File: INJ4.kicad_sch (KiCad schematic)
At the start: 8 parts, among them Q1 VND14NV04-E, Q2 VND14NV04-E, Q3 VND14NV04-E, Q4 VND14NV04-E

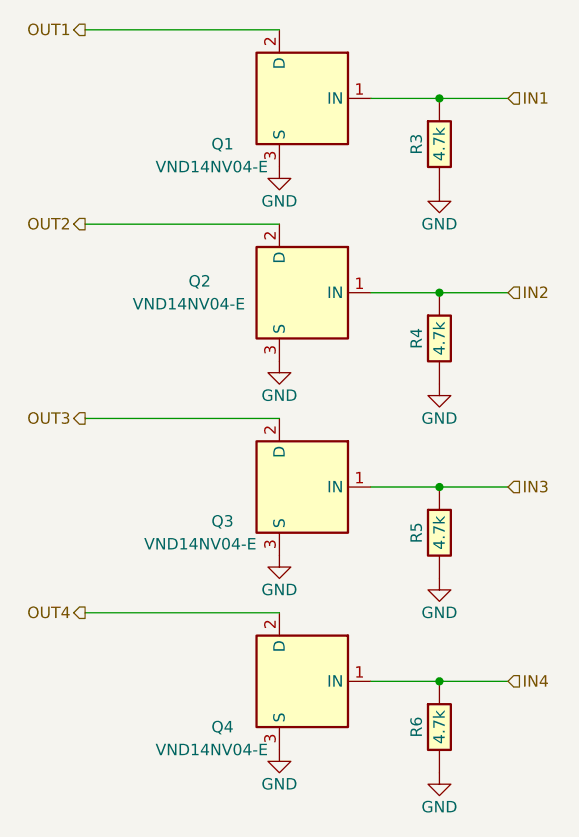
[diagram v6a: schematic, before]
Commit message: EmbeddedEra libraries and template, KiCad 10
- Every symbol except the nine Hellen-One modules now comes from the EmbeddedEra library (resistors and 0R links from the generic libraries, PTC fuses, VND14NV04-E, TE 1-1376430-0, Molex 39281143, test pads, proto area, power symbols). Same-pin parts swapped in place; resistors re-placed between their old pin points with short wires. New parts live on library branch sti2004-parts.
- EmbeddedEra project template: worksheet, text variables, net classes with explicit power classes, JLCPCB design rules; template net names for USB, I2C and the K-line UART.
- Migrated all sheets and the board to KiCad 10 (10.0.7).
- tools/sch_overlap_check.py also fails on overlapping symbol bodies and on fields printed across a wire (found the stacked PTC fuses); KiCad 10 hide flags understood.

Verified: connectivity identical to the previous commit (167 nets), only the planned net renames; 0 overlaps on all 10 sheet files; ERC errors unchanged (148); pinout check 99 OK.

Co-Authored-By: Claude Opus 5.5 <noreply@anthropic.com>
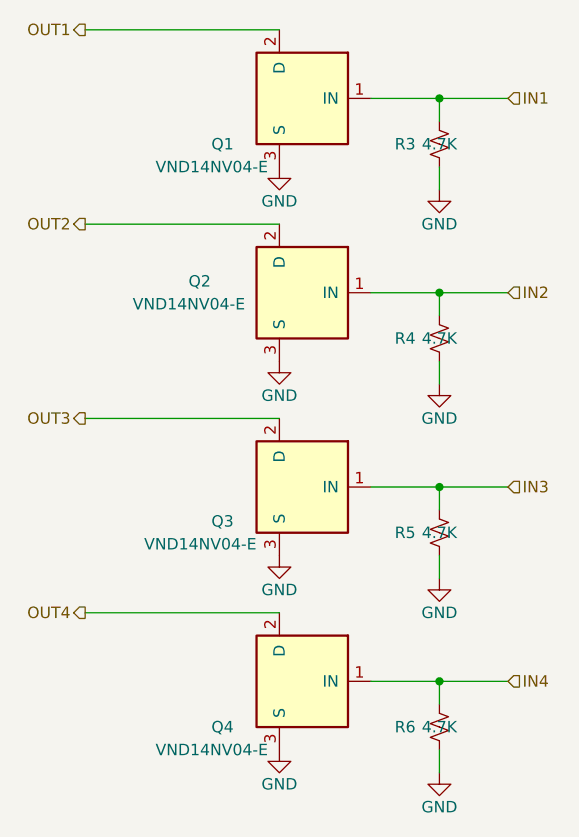
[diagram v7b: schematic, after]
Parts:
- Q1, Q3, Q4: footprint hellen-one-common:DPAK -> EmbeddedEra_Library:TO-252-2; symbol Power_Management:AUIPS2041L -> EmbeddedEra:VND14NV04-E; Manufacturer (none) -> STMicroelectronics; Manufacturer Part Number (none) -> VND14NV04-E
- Q2: footprint hellen-one-common:DPAK -> EmbeddedEra_Library:TO-252-2; symbol Power_Management:AUIPS2041L -> EmbeddedEra:VND14NV04-E; LCSC C155647 -> C155647; Manufacturer (none) -> STMicroelectronics; Manufacturer Part Number (none) -> VND14NV04-E
- R3, R4, R5, R6: value 4.7k -> 4.7K; footprint hellen-one-common:R0603 -> EmbeddedEra_Library:R_0603_1608Metric; symbol hellen-one-common:Res -> EmbeddedEra_Resistors_0603:EE_R_0603_4.7K_1%; LCSC C23162 -> C99782; Manufacturer (none) -> YAGEO; Manufacturer Part Number (none) -> RC0603FR-074K7L
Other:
- moved on the sheet: R3, R4, R5, R6
